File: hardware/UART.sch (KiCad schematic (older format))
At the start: 9 parts, among them J4 DB9_Female_MountingHoles, U14 MAX202

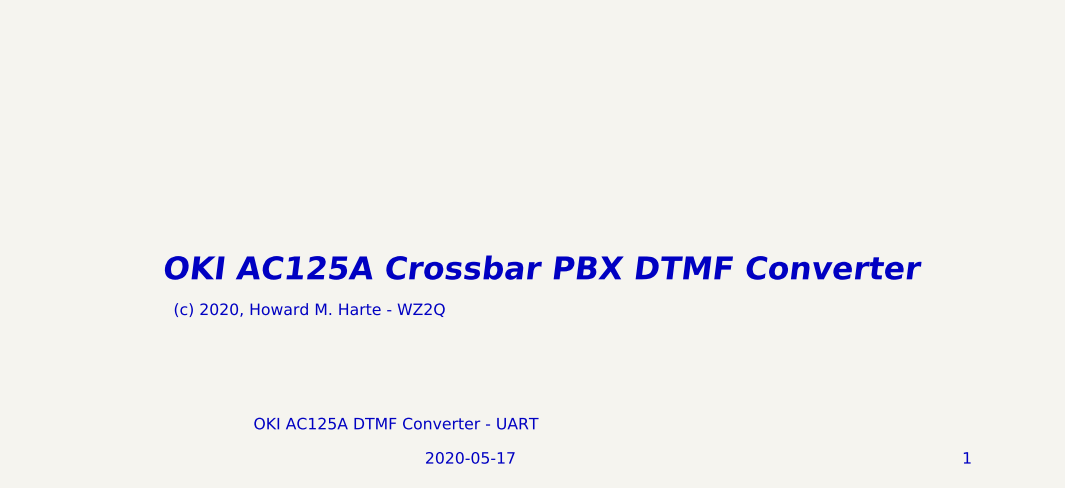
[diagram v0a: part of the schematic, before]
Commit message: Final schematic and PCB layout for Issue 2.
Corrected errors in Issue 1 and fabbed out the PCB.
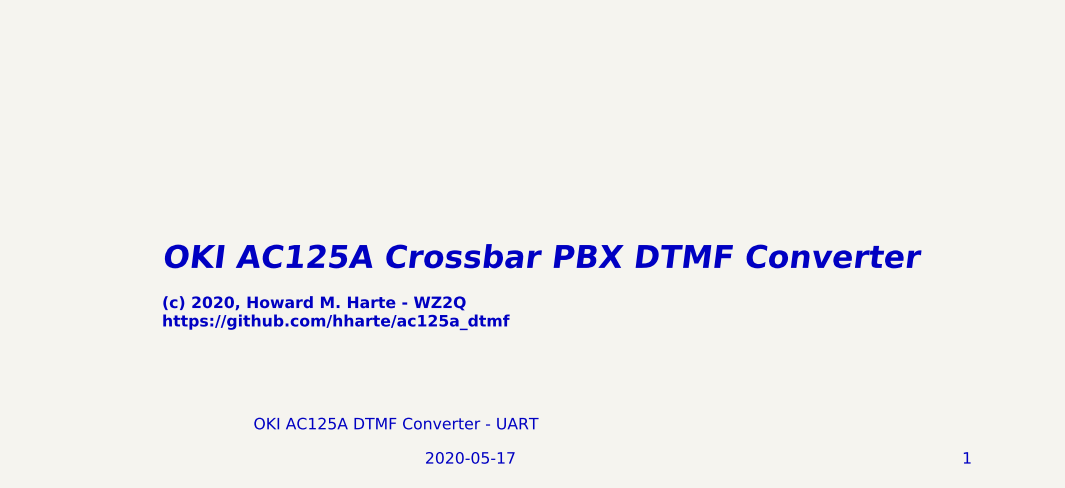
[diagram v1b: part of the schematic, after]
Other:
- note added: "(c) 2020, Howard M. Harte - WZ2Q\nhttps://github.com/hharte/ac125a_dtmf"
- note removed: "(c) 2020, Howard M. Harte - WZ2Q"
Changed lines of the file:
@@
 Text Notes 8250 7650 0    50   ~ 0
 2020-05-17
-Text Notes 7100 6850 0    100  Italic 20
+Text Notes 7100 6800 0    100  Italic 20
 OKI AC125A Crossbar PBX DTMF Converter
-Text Notes 7150 7000 0    50   ~ 0
-(c) 2020, Howard M. Harte - WZ2Q
+Text Notes 7100 7050 0    50   ~ 10
+(c) 2020, Howard M. Harte - WZ2Q\nhttps://github.com/hharte/ac125a_dtmf
 $EndSCHEMATC
